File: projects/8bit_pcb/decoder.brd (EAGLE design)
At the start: 100 x 80 mm, 94 parts, among them IC1 28C64AP, IC2 28C64AP, IC3 28C64AP, IC4 28C64AP, IC5 74LS139N, IC6 74LS139N

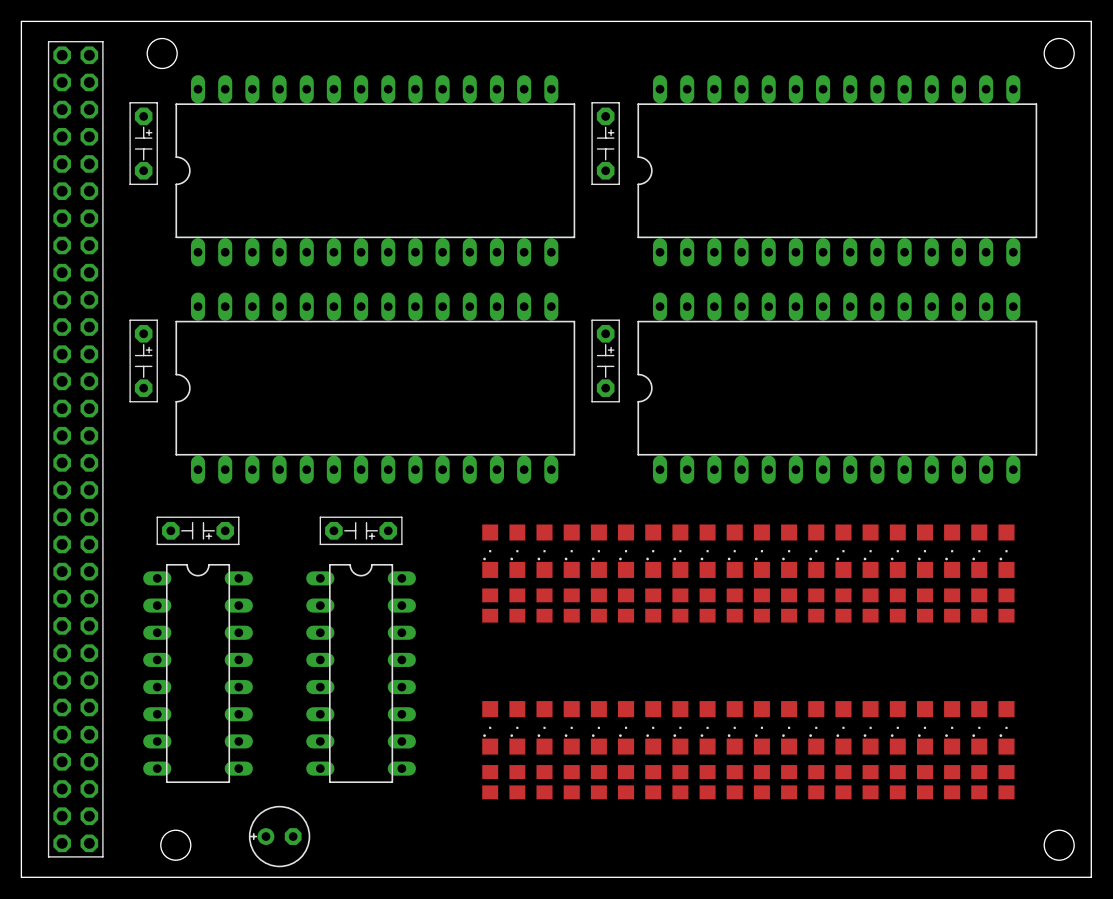
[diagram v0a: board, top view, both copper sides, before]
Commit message: RAM, Disp16Seg, Decoder
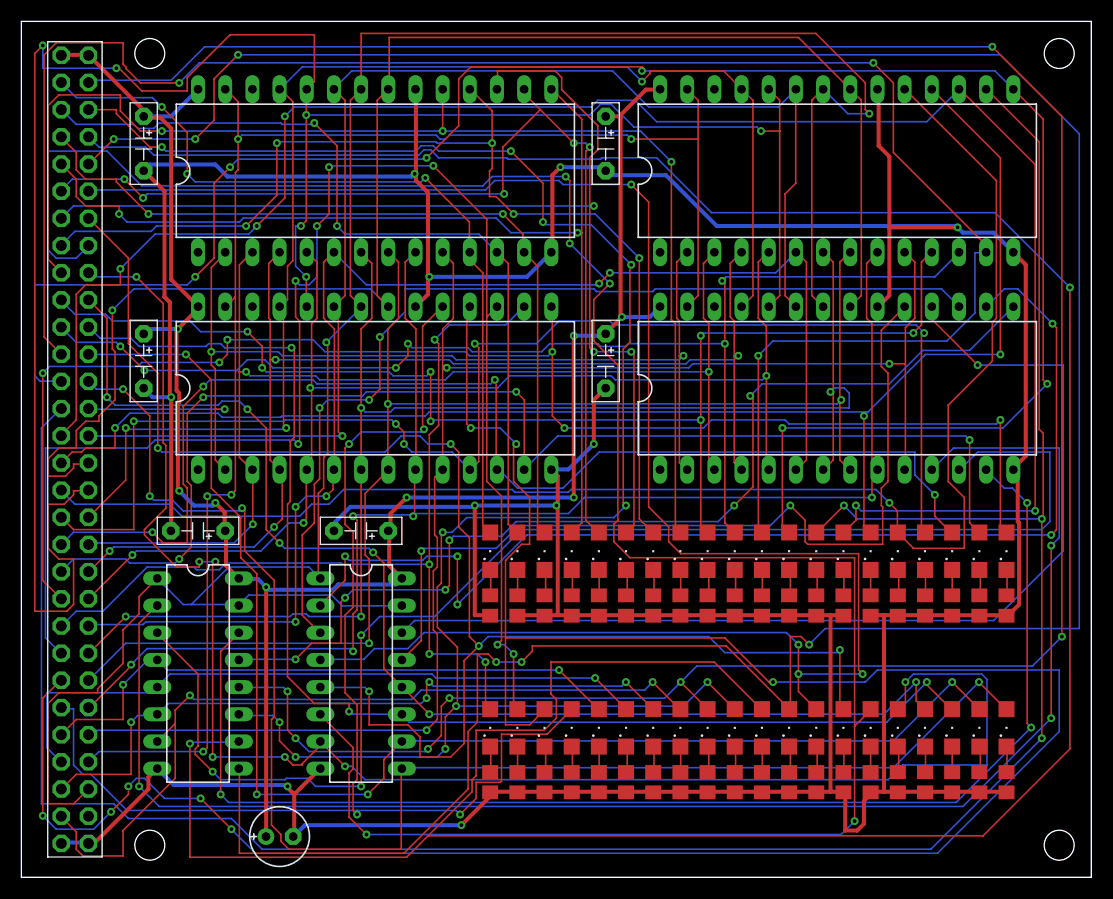
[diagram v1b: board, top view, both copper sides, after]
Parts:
- moved U$1 1.27 mm to (5.00, 40.0)
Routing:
- net GND: track 0.00 -> 459.7 mm, vias 0 -> 10
- net D30: track 0.00 -> 289.6 mm, vias 0 -> 2
- net D31: track 0.00 -> 260.8 mm, vias 0 -> 6
- net D28: track 0.00 -> 234.9 mm, vias 0 -> 7
- net D22: track 0.00 -> 227.7 mm, vias 0 -> 8
- net D12: track 0.00 -> 222.9 mm, vias 0 -> 3
- net D34: track 0.00 -> 210.9 mm, vias 0 -> 5
- net !OE: track 0.00 -> 202.6 mm, vias 0 -> 2
- net A9: track 0.00 -> 197.8 mm, vias 0 -> 6
- net VCC: track 0.00 -> 184.3 mm, vias 0 -> 8
- net D11: track 0.00 -> 184.2 mm, vias 0 -> 6
- net D10: track 0.00 -> 177.5 mm, vias 0 -> 3
- net D32: track 0.00 -> 174.7 mm, vias 0 -> 4
- net D13: track 0.00 -> 173.6 mm, vias 0 -> 5
- net D29: track 0.00 -> 172.6 mm, vias 0 -> 11
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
